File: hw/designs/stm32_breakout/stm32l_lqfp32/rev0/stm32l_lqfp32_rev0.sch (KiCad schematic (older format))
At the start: 15 parts, among them J1 USB_B_Micro, U1 LM3670MF, U3 KC2016Z

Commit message: Updated with BOM and PDF folders
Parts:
- added C?: 100nF, Capacitor_SMD:C_0805_2012Metric, symbol pspice:CAP
- added J2: Conn_ARM_JTAG_SWD_10, symbol Connector:Conn_ARM_JTAG_SWD_10
- added J3, J4: Conn_01x13_Female, symbol Connector:Conn_01x13_Female
- C1: Part_Number (none) -> TMK212ABJ475MG-T
- C2, C4: Part_Number (none) -> JMK212ABJ106KG-T
- C3, C5: Part_Number (none) -> CGA4J2X7R2A104K125AA
- C6: Part_Number (none) -> C0805C105M8RACAUTO
- D1: Part_Number (none) -> XZUR54W-1
- J1: Part_Number (none) -> 47346-0001
- L1: value INDUCTOR -> 10uH
- R1: Part_Number (none) -> ERJ-PB6D2000V
- R2: Part_Number (none) -> RCS08050000Z0EA
- R3: Part_Number (none) -> UNPOP
- U1: value LM3670MF -> LM3670MF-3.3; Part_Number (none) -> LM3670MF-3.3
- U2: renamed from U?; A1_MIN 0.1 -> (none); A_MAX 1.6 -> (none); B_MAX 0.45 -> (none); B_MIN 0.3 -> (none); B_NOM 0.375 -> (none); D1_MAX 7.2 -> (none); D1_MIN 6.8 -> (none); D1_NOM 7.0 -> (none); D2_NOM 0.0 -> (none); D_MAX 9.2 -> (none); D_MIN 8.8 -> (none); D_NOM 9.0 -> (none); E1_MAX 7.2 -> (none); E1_MIN 6.8 -> (none); E1_NOM 7.0 -> (none); E2_NOM 0.0 -> (none); ENOM 0.8 -> (none); E_MAX 9.2 -> (none); E_MIN 8.8 -> (none); E_NOM 9.0 -> (none); L_MAX 0.75 -> (none); L_MIN 0.45 -> (none); L_NOM 0.6 -> (none); MANUFACTURER STMicroelectronics -> (none); PARTREV 3 -> (none); PIN_COUNT_D 8.0 -> (none); PIN_COUNT_E 8.0 -> (none); Part_Number (none) -> STM32L010K4T6; STANDARD IPC 7351B -> (none)
- U3: Part_Number (none) -> KC2016Z32.0000C15XXK
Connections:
- net +3V3: now also J2.1 (VTref), J4.1 (Pin_1)
- net GND: now also U2.16 (VSS), U2.32 (VSS), C?.1, J2.3 (GND), J2.5 (GND), J2.9 (GNDDetect), J3.1 (Pin_1)
- net NRST: now also J2.10 (~RESET~)
- net PA-CK_IN: now also J4.4 (Pin_4)
- net PA1: now also J4.5 (Pin_5)
- net PA10: now also J3.2 (Pin_2)
- net PA11: now also J3.3 (Pin_3)
- net PA12: now also J3.4 (Pin_4)
- net PA13-SWDIO: now also J2.2 (SWDIO/TMS), J3.5 (Pin_5)
- net PA14-SWCLK: now also J2.4 (SWDCLK/TCK), J3.6 (Pin_6)
- net PA15: now also J3.7 (Pin_7)
- net PA2: now also J4.6 (Pin_6)
- net PA3: now also J4.7 (Pin_7)
- net PA4: now also J4.8 (Pin_8)
- net PA5: now also J4.9 (Pin_9)
- net PA6: now also J4.10 (Pin_10)
- net PA7: now also J4.11 (Pin_11)
- net PA8: now also J4.12 (Pin_12)
- net PA9: now also J4.13 (Pin_13)
- net PB3: now also J3.8 (Pin_8)
- net PB4: now also J3.9 (Pin_9)
- net PB5: now also J3.10 (Pin_10)
- net PB6: now also J3.11 (Pin_11)
- net PB7: now also J3.12 (Pin_12)
- net PB9-BOOT0: now also J3.13 (Pin_13)
- net PC14: now also J4.2 (Pin_2)
- net PC15: now also J4.3 (Pin_3)
- net at C2.2, C3.2, C4.2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: now also C?.2
- no-connect marks 5 -> 6
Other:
- note added: "TODO: Add Cable assembly for 20pin to 10pin cable"
- note added: "V(f) = 2V\nI=V/R=3V/200=15mA"
- moved on the sheet: C1, C2, C3, C4, C5, C6, D1, J1, L1, R1, R2, R3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

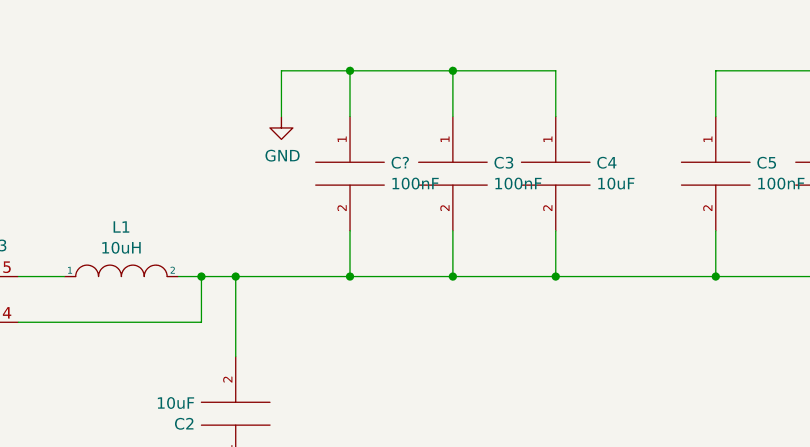
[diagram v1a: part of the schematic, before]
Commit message: Part number was missing for inductor
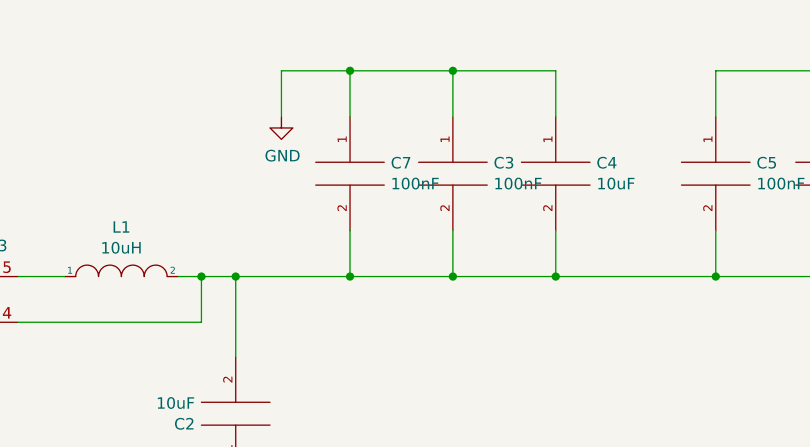
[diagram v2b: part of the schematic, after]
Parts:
- J2: footprint (none) -> Custom:2X05_1.27MM_BOX_POSTS
- J3, J4: footprint (none) -> Connector_PinHeader_2.54mm:PinHeader_1x13_P2.54mm_Vertical
- L1: Part_Number (none) -> LB3218T100K
- gave numbers to parts that had none: 1
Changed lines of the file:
@@
 F 1 "KC2016Z" H 9444 2155 50  0000 L CNN
 F 2 "Custom:KC2016Z" H 9150 2350 50  0001 C CNN
-F 3 "https://global.kyocera.com/prdct/electro/product/pdf/clock_z_xz_e.pdf" H 9150 2350 50  0001 C CNN
+F 3 "https://ele.kyocera.com/assets/products/crystal-device/clock_z_x_e.pdf" H 9150 2350 50  0001 C CNN
 F 4 "KC2016Z32.0000C15XXK" H 9500 1950 50  0000 C CNN "Part_Number"
 	1    9000 2200
@@
 F 1 "10uH" H 3550 1974 50  0000 C CNN
 F 2 "Inductor_SMD:L_1210_3225Metric_Pad1.42x2.65mm_HandSolder" H 3550 1850 50  0001 C CNN
-F 3 "~" H 3550 1850 50  0001 C CNN
+F 3 "https://ds.yuden.co.jp/TYCOMPAS/ut/detail?pn=LB3218T100K%20%20&u=M" H 3550 1850 50  0001 C CNN
+F 4 "LB3218T100K" H 3550 1850 50  0001 C CNN "Part_Number"
 	1    3550 1850
 	1    0    0    -1
@@
 F 0 "J4" H 10028 4276 50  0000 L CNN
 F 1 "Conn_01x13_Female" H 10028 4185 50  0000 L CNN
-F 2 "" H 10000 4250 50  0001 C CNN
+F 2 "Connector_PinHeader_2.54mm:PinHeader_1x13_P2.54mm_Vertical" H 10000 4250 50  0001 C CNN
 F 3 "~" H 10000 4250 50  0001 C CNN
 F 4 "PREC013SAAN-RC" H 9500 3550 50  0000 C CNN "Part_Number"
@@
 F 0 "J3" H 3078 4426 50  0000 L CNN
 F 1 "Conn_01x13_Female" H 3078 4335 50  0000 L CNN
-F 2 "" H 3050 4400 50  0001 C CNN
+F 2 "Connector_PinHeader_2.54mm:PinHeader_1x13_P2.54mm_Vertical" H 3050 4400 50  0001 C CNN
 F 3 "~" H 3050 4400 50  0001 C CNN
 F 4 "PREC013SAAN-RC" H 2500 3750 50  0000 C CNN "Part_Number"
@@
 F 0 "J2" H 2157 6491 50  0000 R CNN
 F 1 "Conn_ARM_JTAG_SWD_10" H 2157 6400 50  0000 R CNN
-F 2 "" H 2600 6400 50  0001 C CNN
+F 2 "Custom:2X05_1.27MM_BOX_POSTS" H 2600 6400 50  0001 C CNN
 F 3 "https://www.adafruit.com/product/4048#description" V 2250 5150 50  0001 C CNN
 F 4 "4048" H 3150 5800 50  0000 R CNN "Part_Number"
@@
 TODO: Add Cable assembly for 20pin to 10pin cable
 $Comp
-L pspice:CAP C?
+L pspice:CAP C7
 U 1 1 6165B9B5
 P 4550 1400
-F 0 "C?" H 4728 1446 50  0000 L CNN
+F 0 "C7" H 4728 1446 50  0000 L CNN
 F 1 "100nF" H 4728 1355 50  0000 L CNN
 F 2 "Capacitor_SMD:C_0805_2012Metric" H 4550 1400 50  0001 C CNN
